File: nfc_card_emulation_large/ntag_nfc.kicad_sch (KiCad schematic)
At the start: 1 part, among them U2 NT3H2x11

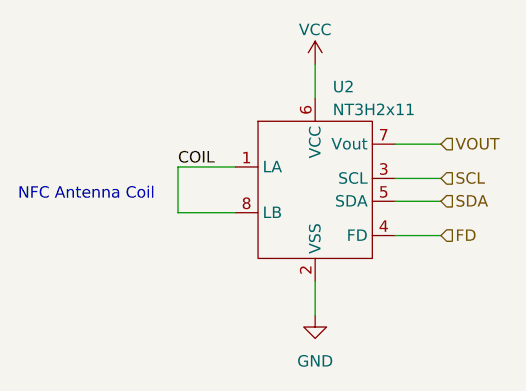
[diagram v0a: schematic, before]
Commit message: Added front artwork to nfc_card_emulation_large
Also created BOM and pos files
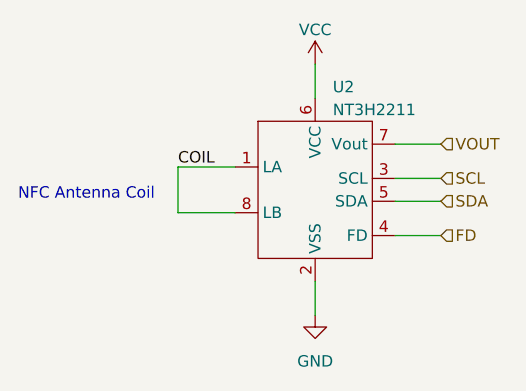
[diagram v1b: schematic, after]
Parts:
- U2: value NT3H2x11 -> NT3H2211
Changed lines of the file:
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@@
   (title_block
     (title "NFC NTAG I2C tag")
-    (date "2023-05-07")
+    (date "2023-06-22")
     (rev "1.0")
     (comment 1 "CC-BY-SA")
@@
     (pin "1")
     (instances
-      (project "nfc_card_emulation"
+      (project "nfc_card_emulation_large"
         (path "/01149b17-33ef-4823-97dd-2a81938478fb/dcc1f91b-33ec-4f9d-b582-080400b05bca"
           (reference "#PWR02") (unit 1)
@@
     (pin "1")
     (instances
-      (project "nfc_card_emulation"
+      (project "nfc_card_emulation_large"
         (path "/01149b17-33ef-4823-97dd-2a81938478fb/dcc1f91b-33ec-4f9d-b582-080400b05bca"
           (reference "#PWR01") (unit 1)
@@
       (effects (font (size 1.27 1.27)) (justify left))
     )
-    (property "Value" "NT3H2x11" (at 103.5559 76.2 0)
+    (property "Value" "NT3H2211" (at 103.5559 76.2 0)
       (effects (font (size 1.27 1.27)) (justify left))
     )
@@
     (pin "8")
     (instances
-      (project "nfc_card_emulation"
+      (project "nfc_card_emulation_large"
         (path "/01149b17-33ef-4823-97dd-2a81938478fb/dcc1f91b-33ec-4f9d-b582-080400b05bca"
           (reference "U2") (unit 1)
